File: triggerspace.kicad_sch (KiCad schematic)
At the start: 135 parts, among them J1 Conn_01x2, J10 Conn_01x12, J11 Conn_01x12, J12 Conn_02x05_Odd_Even, J13 Conn_01x10, J14 Conn_01x10, J15 Conn_01x10, J2 Conn_01x2, J3 Conn_01x4, J4 Conn_01x4, J5 Conn_01x3, J6 Conn_01x3, J7 Conn_01x10, J8 Conn_01x3, J9 Conn_01x2, Q1 2N3904, Q2 2N3904, U1 MCP6002_1, U2 MCP6002_1, U3 MCP6002_1, U4 L7805, U5 LM4040LP-5, U6 74HC595, U8 6N138, X1 CV_X, Y1 CV_Y

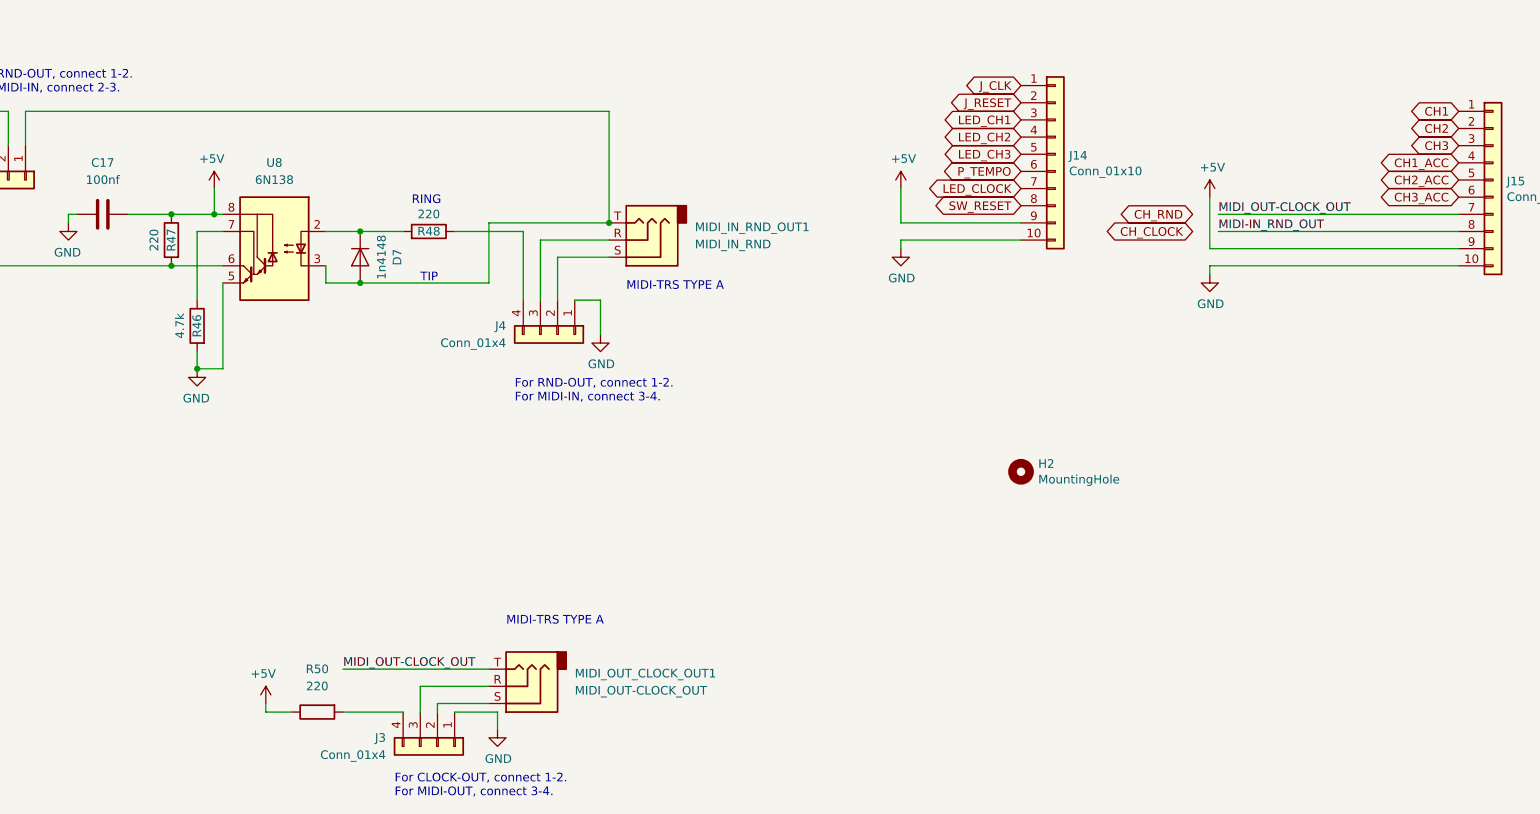
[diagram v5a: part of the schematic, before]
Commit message: LPZW auto-crossover MIDI IN (TRS Type A/B) with SOIC-8 and 6N138 build options
U8 becomes an HCPL-2630 dual optocoupler wired as the LPZW auto-crossover
MIDI input (Kay Knofe / LPZW.modules, credited on the jack PCB silkscreen):
two anti-parallel LEDs across tip and ring with their own 220R (R48, new
R51), wire-ORed open-collector outputs, pull-up R47 220R -> 1k.

- U9: optional HCPL-0630 SOIC-8 footprint inside U8's DIP-8 footprint
- JP3/JP4 3-pad solder jumpers (1-2 bridged) and optional D7 keep a
  6N138 build possible (cut 1-2, bridge 2-3, fit D7)
- R46 to 5.08mm pitch; D7 moved and DNP; local re-place/re-route around U8
- README: Build options section; CHANGELOG v0.5.0 entries
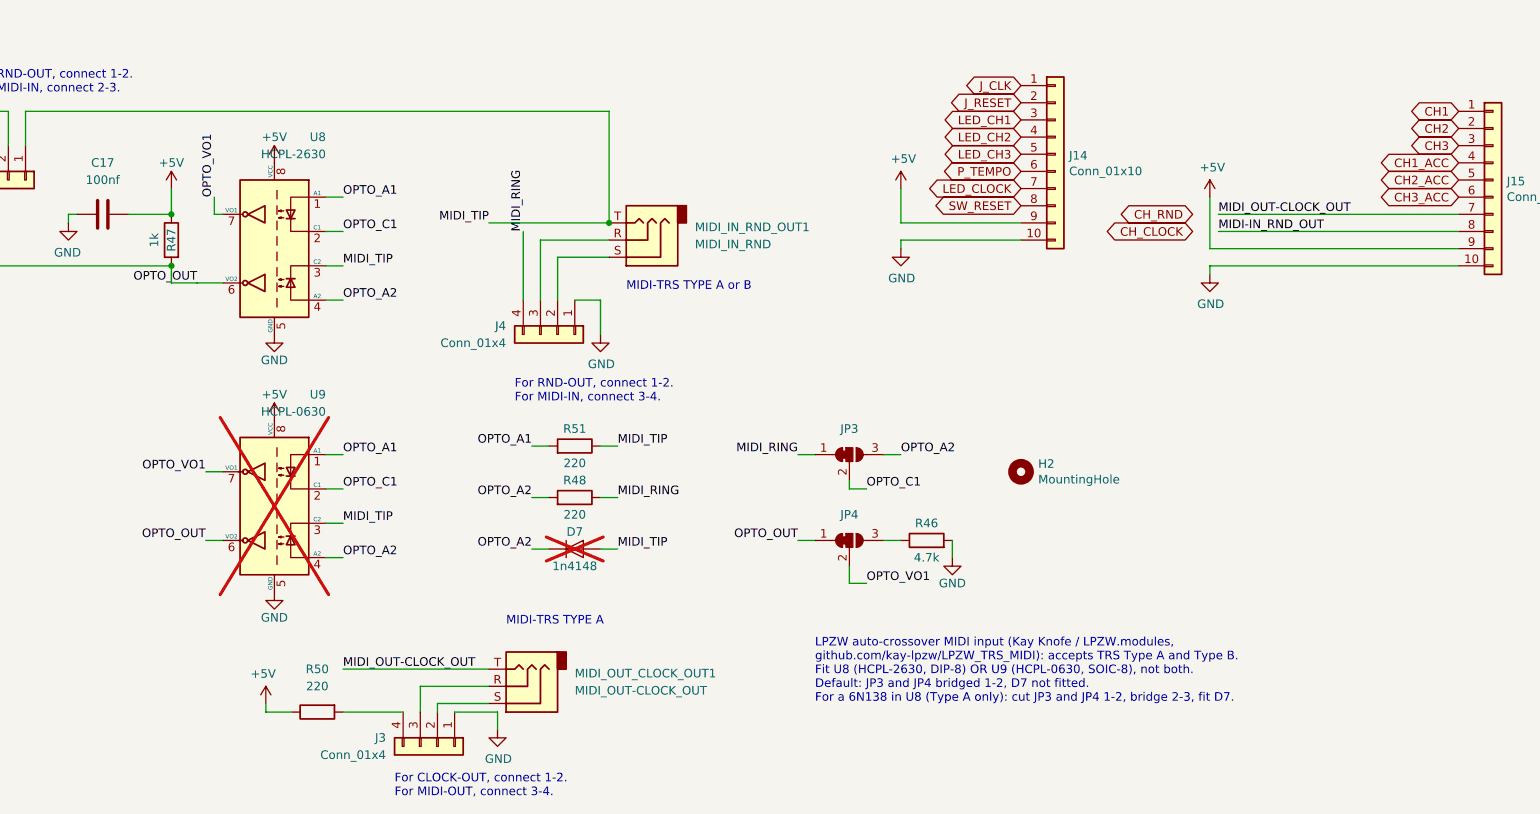
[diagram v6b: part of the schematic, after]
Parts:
- added JP3, JP4: SolderJumper_3_Bridged12, Jumper:SolderJumper-3_P1.3mm_Bridged12_RoundedPad1.0x1.5mm_NumberLabels, symbol Jumper:SolderJumper_3_Bridged12
- added R51: 220, Resistor_THT:R_Axial_DIN0204_L3.6mm_D1.6mm_P7.62mm_Horizontal, symbol NanoGris-rescue:R-Device-GridsNanoV3-rescue
- added U9: HCPL-0630, Package_SO:SOIC-8_3.9x4.9mm_P1.27mm, symbol Isolator:HCPL-0630
- D7: now not fitted
- R46: footprint Resistor_THT:R_Axial_DIN0204_L3.6mm_D1.6mm_P7.62mm_Horizontal -> Resistor_THT:R_Axial_DIN0204_L3.6mm_D1.6mm_P5.08mm_Horizontal
- R47: value 220 -> 1k
- U8: value 6N138 -> HCPL-2630; symbol Isolator:6N138 -> Isolator:HCPL-2630
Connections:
- net +5V: now also U9.8 (VCC)
- net GND: now also U9.5 (GND)
- net MIDI_TIP: now reaches D7.2 (A), J8.1 (Pin_1), MIDI_IN_RND_OUT1.T, U8.3 (C2)
- net MIDI_TIP: now also R51.1, U9.3 (C2)
- net OPTO_A1: now reaches U8.1 (A1)
- net OPTO_A1: now also R51.2, U9.1 (A1)
- net OPTO_A2: now reaches D7.1 (K), R48.2
- net OPTO_A2: now also U8.4 (A2), JP3.3 (B), U9.4 (A2); no longer U8.2 (C1)
- net OPTO_OUT: now reaches J8.3 (Pin_3), R47.2, U8.6 (VO2)
- net OPTO_OUT: now also JP4.1 (A), U9.6 (VO2)
- net at R46.1: now also JP4.3 (B); no longer U8.7 (VO1)
- net MIDI_RING: now reaches J4.4 (Pin_4), R48.1
- net MIDI_RING: now also JP3.1 (A)
- new net OPTO_C1: JP3.2 (C), U8.2 (C1), U9.2 (C1)
- new net OPTO_VO1: JP4.2 (C), U8.7 (VO1), U9.7 (VO1)
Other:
- note added: "LPZW auto-crossover MIDI input (Kay Knofe / LPZW.modules, github.com/kay-lpzw/LPZW_TRS_MIDI): accepts TRS Type A and Type B. Fit U8 (HCPL-2630, DIP-8) OR U9 (HCPL-0630, SOIC-8), not both. Default: JP3 and JP4 bridged 1-2, D7 not fitted. For a 6N138 in U8 (Type A only): cut JP3 and JP4 1-2, bridge 2-3, fit D7."
- note added: "MIDI-TRS TYPE A or B"
- note removed: "RING"
- note removed: "TIP"
- moved on the sheet: R46, R48
